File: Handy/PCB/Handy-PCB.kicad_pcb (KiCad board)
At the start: 2 copper layers, 163.8 x 126.2 mm, 1 part

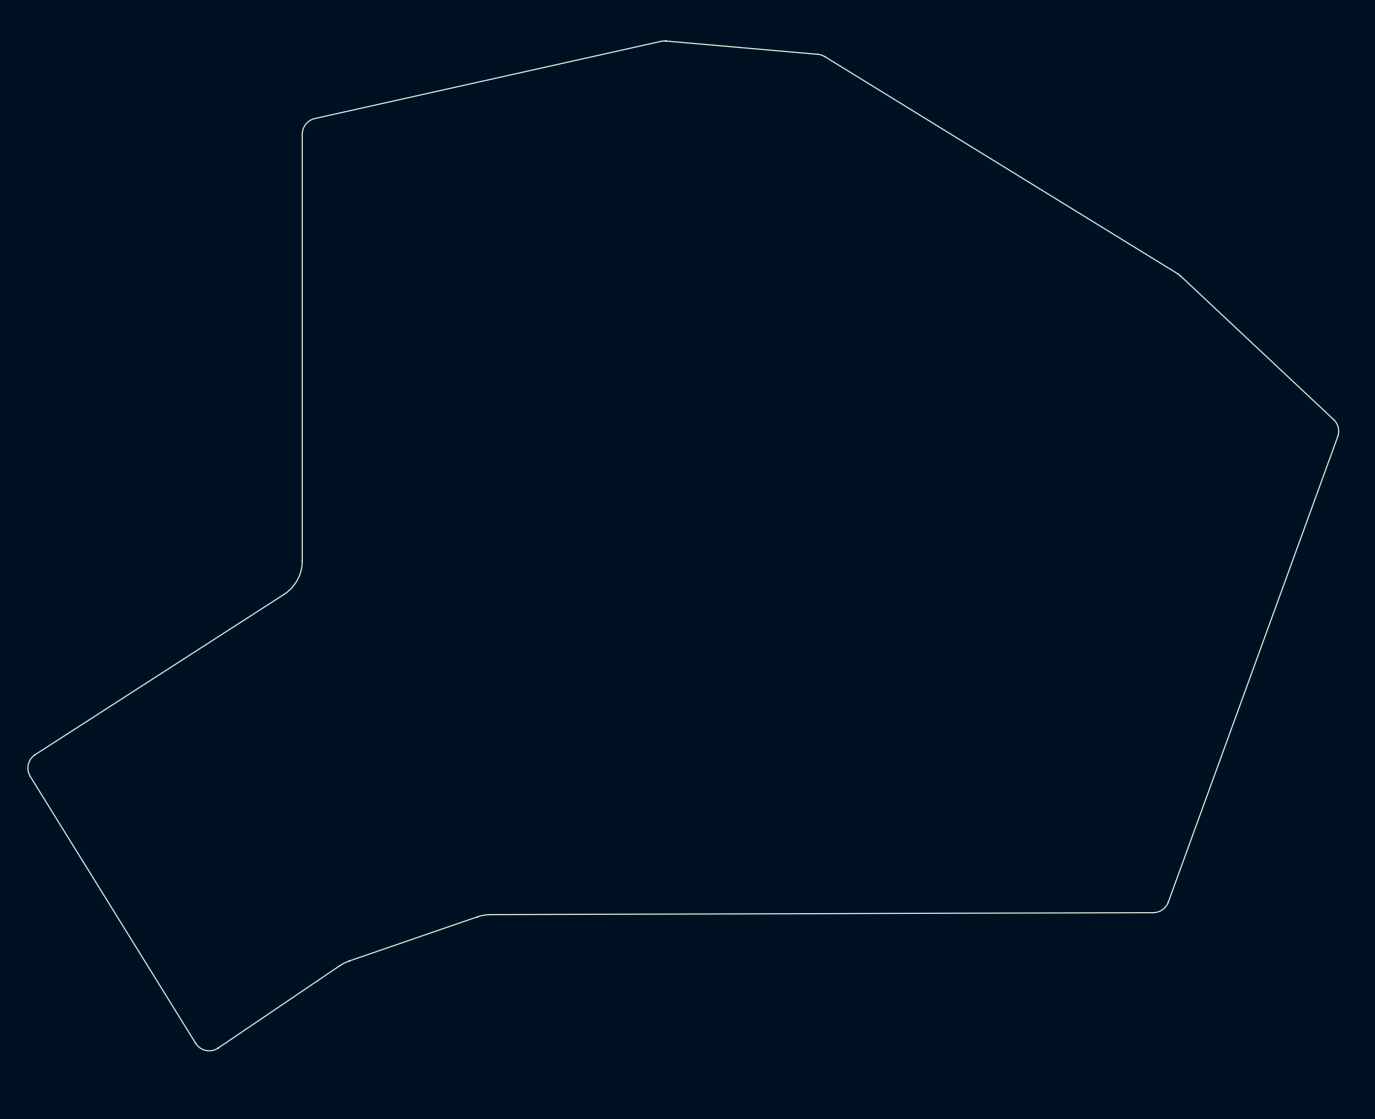
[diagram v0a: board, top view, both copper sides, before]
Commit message: KiCad/Handy: Placing/updating keys' footprints on PCB
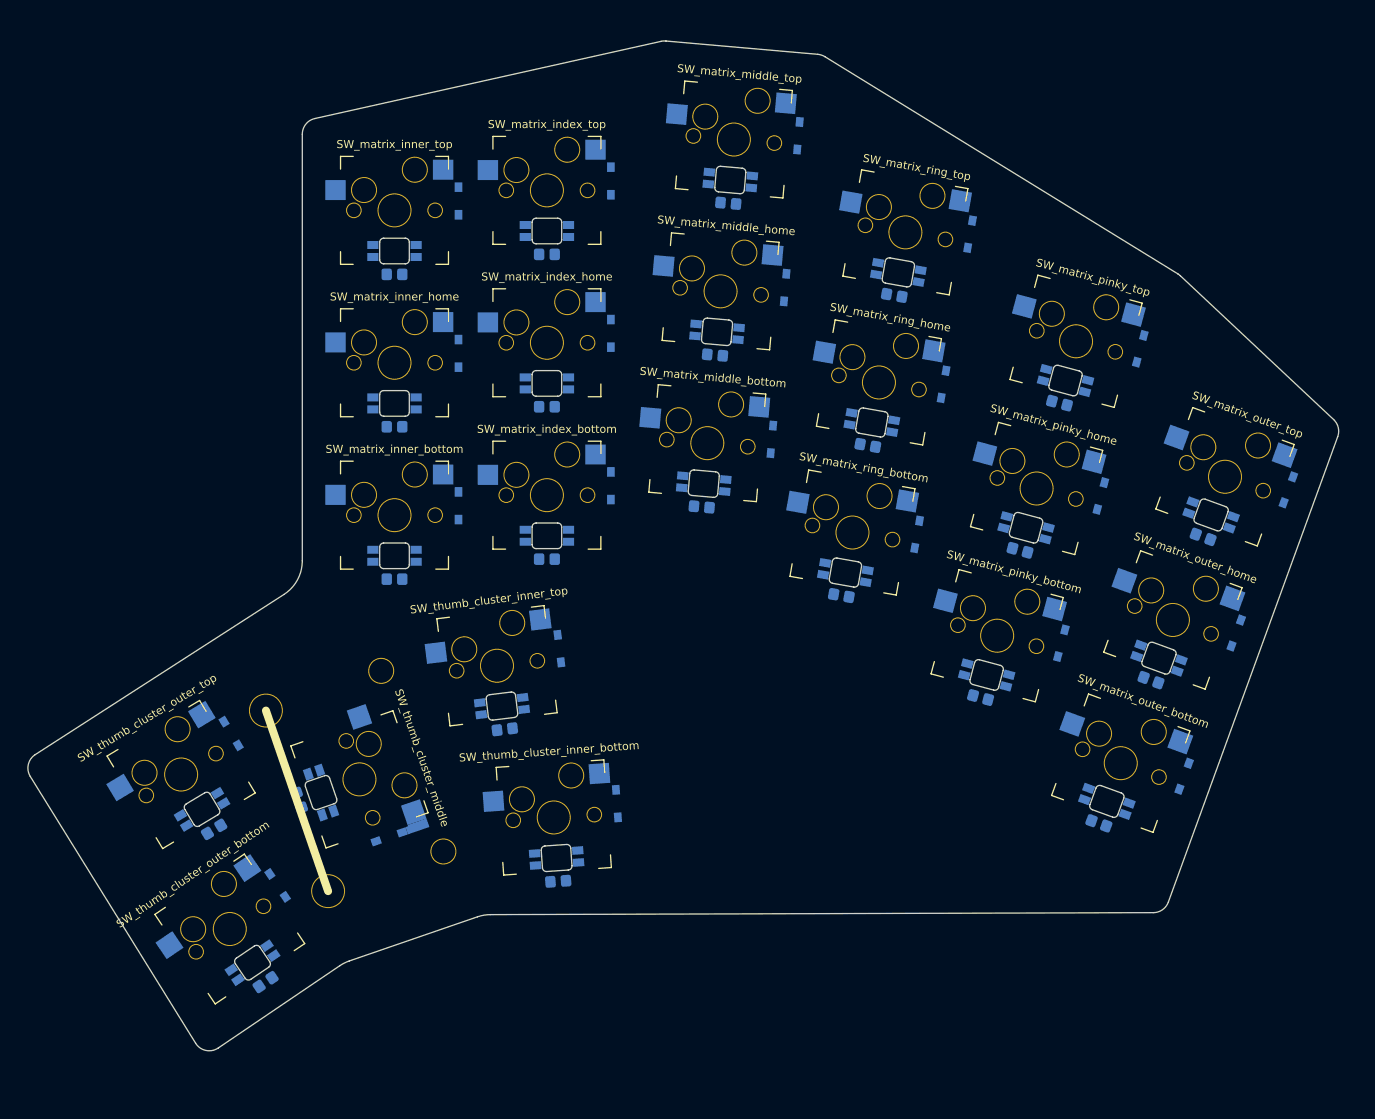
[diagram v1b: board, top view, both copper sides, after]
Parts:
- added SW_matrix_index_bottom: Cherry MX 1u, Keebs:CherryMX_1u_with_smd_diode, F.Cu at (139.1, 87.5)
- added SW_matrix_index_home: Cherry MX 1u, Keebs:CherryMX_1u_with_smd_diode, F.Cu at (139.1, 68.5)
- added SW_matrix_index_top: Cherry MX 1u, Keebs:CherryMX_1u_with_smd_diode, F.Cu at (139.1, 49.4)
- added SW_matrix_inner_bottom: Cherry MX 1u, Keebs:CherryMX_1u_with_smd_diode, F.Cu at (120.0, 90.0)
- added SW_matrix_inner_home: Cherry MX 1u, Keebs:CherryMX_1u_with_smd_diode, F.Cu at (120.0, 71.0)
- added SW_matrix_inner_top: Cherry MX 1u, Keebs:CherryMX_1u_with_smd_diode, F.Cu at (120.0, 51.9)
- added SW_matrix_middle_bottom: Cherry MX 1u, Keebs:CherryMX_1u_with_smd_diode, F.Cu at (159.1, 81.0)
- added SW_matrix_middle_home: Cherry MX 1u, Keebs:CherryMX_1u_with_smd_diode, F.Cu at (160.8, 62.0)
- added SW_matrix_middle_top: Cherry MX 1u, Keebs:CherryMX_1u_with_smd_diode, F.Cu at (162.4, 43.0)
- added SW_matrix_outer_bottom: Cherry MX 1u, Keebs:CherryMX_1u_with_smd_diode, F.Cu at (210.8, 121.0)
- added SW_matrix_outer_home: Cherry MX 1u, Keebs:CherryMX_1u_with_smd_diode, F.Cu at (217.3, 103.1)
- added SW_matrix_outer_top: Cherry MX 1u, Keebs:CherryMX_1u_with_smd_diode, F.Cu at (223.8, 85.2)
- added SW_matrix_pinky_bottom: Cherry MX 1u, Keebs:CherryMX_1u_with_smd_diode, F.Cu at (195.3, 105.1)
- added SW_matrix_pinky_home: Cherry MX 1u, Keebs:CherryMX_1u_with_smd_diode, F.Cu at (200.3, 86.7)
- added SW_matrix_pinky_top: Cherry MX 1u, Keebs:CherryMX_1u_with_smd_diode, F.Cu at (205.2, 68.3)
- added SW_matrix_ring_bottom: Cherry MX 1u, Keebs:CherryMX_1u_with_smd_diode, F.Cu at (177.2, 92.2)
- added SW_matrix_ring_home: Cherry MX 1u, Keebs:CherryMX_1u_with_smd_diode, F.Cu at (180.6, 73.4)
- added SW_matrix_ring_top: Cherry MX 1u, Keebs:CherryMX_1u_with_smd_diode, F.Cu at (183.9, 54.7)
- added SW_thumb_cluster_inner_bottom: Cherry MX 1u, Keebs:CherryMX_1u_with_smd_diode, F.Cu at (139.9, 127.8)
- added SW_thumb_cluster_inner_top: Cherry MX 1u, Keebs:CherryMX_1u_with_smd_diode, F.Cu at (132.8, 108.8)
- added SW_thumb_cluster_middle: Cherry MX 1u, Keebs:CherryMX_2u_with_smd_diode, F.Cu at (115.6, 123.0)
- added SW_thumb_cluster_outer_bottom: Cherry MX 1u, Keebs:CherryMX_1u_with_smd_diode, F.Cu at (99.4, 141.7)
- added SW_thumb_cluster_outer_top: Cherry MX 1u, Keebs:CherryMX_1u_with_smd_diode, F.Cu at (93.3, 122.4)

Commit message: Handy: Small adjustments to angled  keys proximity to each other
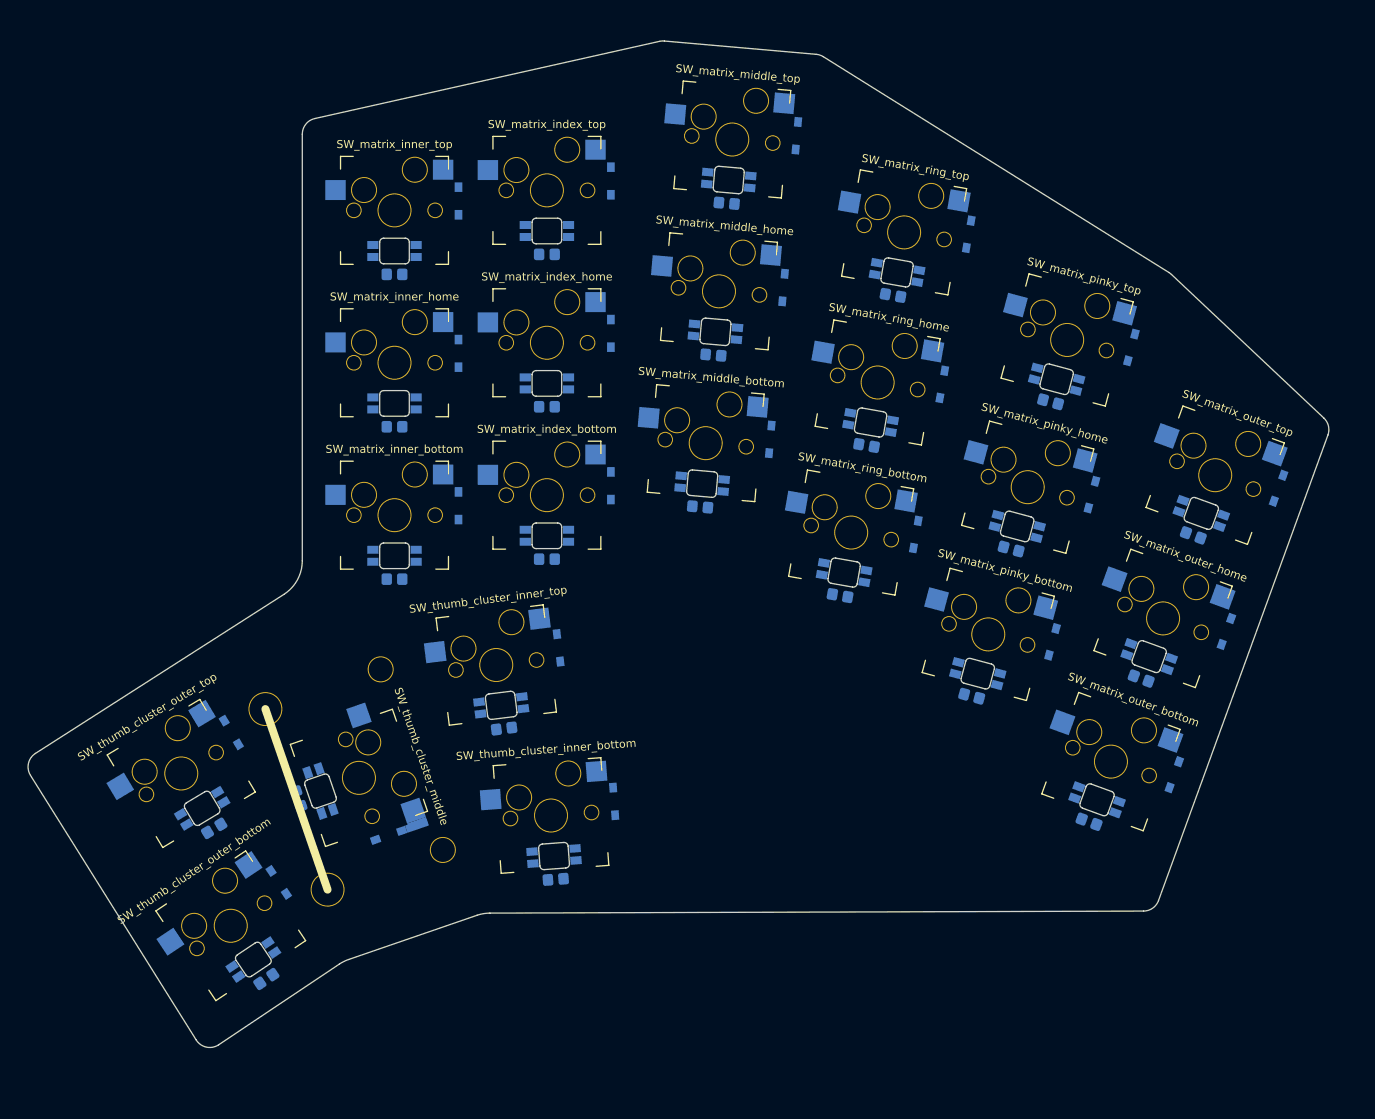
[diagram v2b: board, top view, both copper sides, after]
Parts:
- moved SW_matrix_outer_bottom 1.24 mm to (209.6, 120.8)
- moved SW_matrix_outer_top 1.24 mm to (222.6, 85.0)
- moved SW_matrix_outer_home 1.24 mm to (216.1, 102.9)
- moved SW_matrix_pinky_bottom 1.12 mm to (194.2, 104.9)
- moved SW_matrix_pinky_home 1.12 mm to (199.2, 86.5)
- moved SW_matrix_pinky_top 1.12 mm to (204.1, 68.1)
- moved SW_thumb_cluster_outer_bottom 0.42 mm to (99.5, 141.3), turned to 33.77 degrees
- moved SW_thumb_cluster_inner_bottom 0.42 mm to (139.6, 127.5), turned to 4.23 degrees
- moved SW_thumb_cluster_middle 0.20 mm to (115.6, 122.8)
- moved SW_matrix_middle_top 0.20 mm to (162.2, 43.0)
- moved SW_matrix_middle_bottom 0.20 mm to (158.9, 81.0)
- moved SW_matrix_middle_home 0.20 mm to (160.6, 62.0)
- moved SW_matrix_ring_top 0.16 mm to (183.7, 54.7)
- moved SW_matrix_ring_bottom 0.16 mm to (177.1, 92.2)
- moved SW_matrix_ring_home 0.16 mm to (180.4, 73.4)
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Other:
- board size 163.8 x 126.2 mm -> 162.6 x 125.8 mm

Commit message: Handy: Finally generating a proper outline
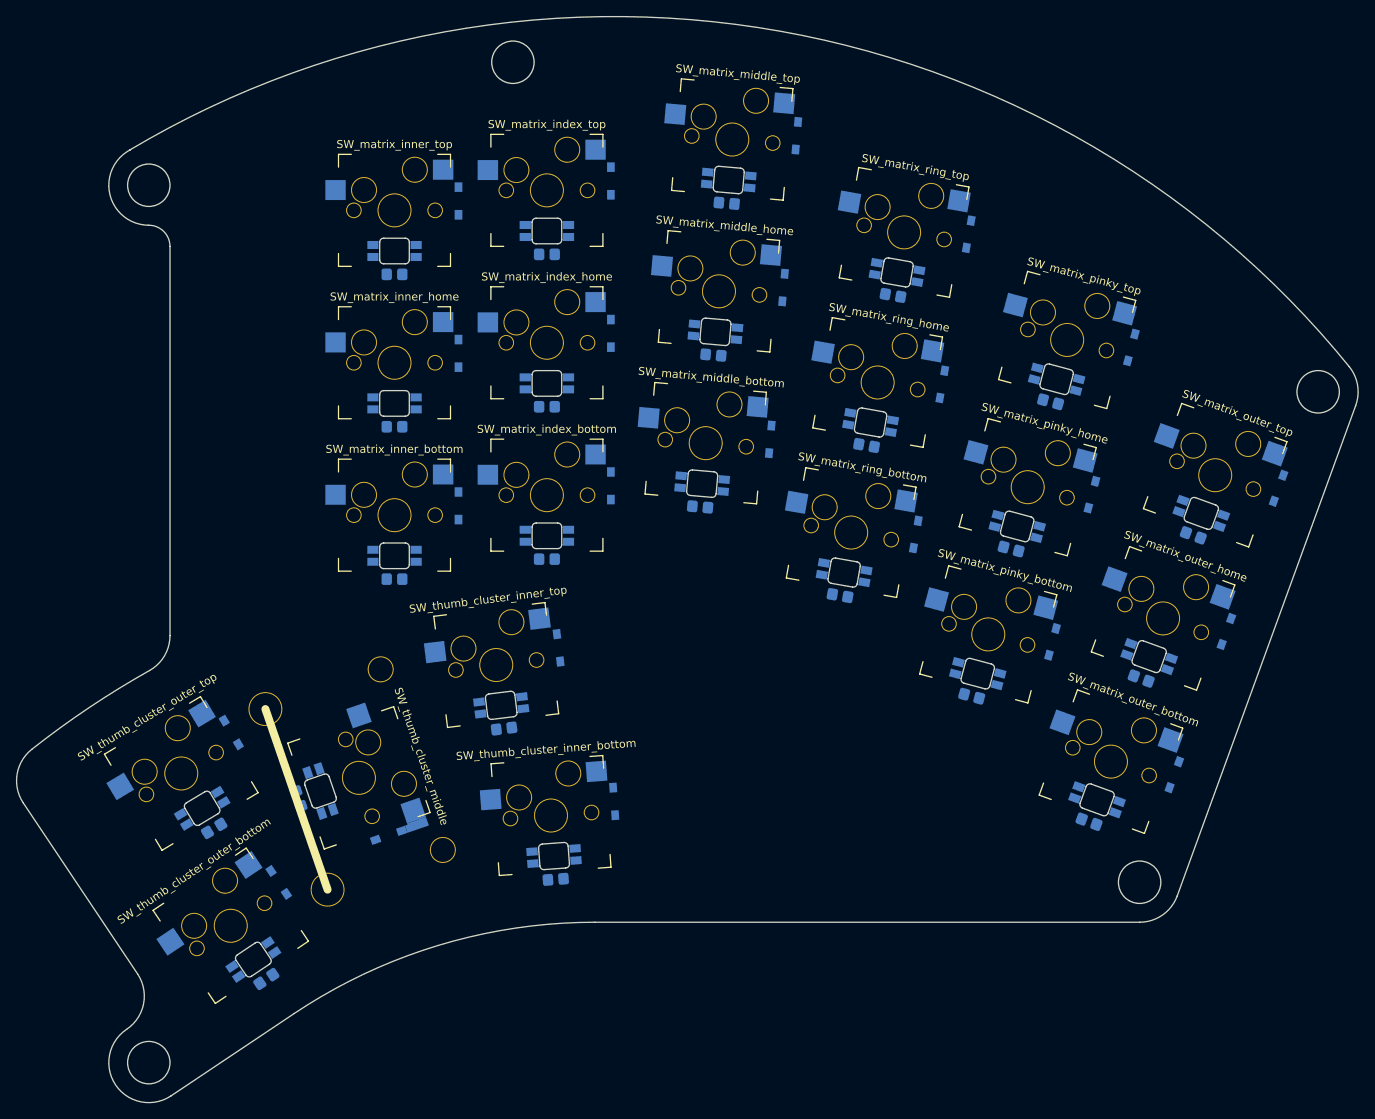
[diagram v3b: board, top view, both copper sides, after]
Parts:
- removed the ECoutline at (120.0, 90.0)
- added ECoutline: Handy-case, Ergogen:Handy-case, F.Cu at (120.0, 90.0)
- added HW__case_tenting_hole_bottom_left: MountingHole_2.2mm_M2_ISO14580, Keebs:M5_with_washer, F.Cu at (89.3, 158.4)
- added HW__case_tenting_hole_bottom_right: MountingHole_2.2mm_M2_ISO14580, Keebs:M5_with_washer, F.Cu at (213.1, 135.9)
- added HW__case_tenting_hole_top_left: MountingHole_2.2mm_M2_ISO14580, Keebs:M5_with_washer, F.Cu at (89.3, 48.8)
- added HW__case_tenting_hole_top_middle: MountingHole_2.2mm_M2_ISO14580, Keebs:M5_with_washer, F.Cu at (134.8, 33.4)
- added HW__case_tenting_hole_top_right: MountingHole_2.2mm_M2_ISO14580, Keebs:M5_with_washer, F.Cu at (235.5, 74.6)
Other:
- board size 162.6 x 125.8 mm -> 167.7 x 135.8 mm
